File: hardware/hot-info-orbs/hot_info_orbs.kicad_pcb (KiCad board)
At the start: 2 copper layers, 198.8 x 28.5 mm, 11 parts, among them SW1 SW_Push, SW2 SW_Push, SW3 SW_Push, U2 ESP32-S3-SuperMini

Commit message: Board fixes: DS5 DC connected, button off the strapping pin, GND pour added
Three changes to Yang's Rev 1.0, all verified against the file and by re-running
KiCad's own checks -- ERC 0, DRC 0, 0 unconnected pads, 0 schematic parity
issues, and the three silkscreen warnings cleared too.

DS5 pin 5 (DC) now lands on Net-(DS1-DC). The wire had been drawn but stopped
3.81mm short of the pin, so the fifth display had no data/command line. Worth
noting DRC could never have caught it: the board faithfully implemented the
schematic, and the gap was in the schematic. Only ERC sees that class.

SW3 moved from GPIO3 to GPIO10. GPIO3 is an ESP32-S3 strapping pin and the
buttons pull high, so holding that button during a reset drove a strapping pin
at boot -- the shape of an intermittent no-boot nobody traces to a button.
GPIO10 was already broken out and unused.

GND pour on B.Cu, and a SECOND antenna keepout added on B.Cu. The original
keepout was F.Cu only and set to copperpour allowed, so a back-side pour would
have filled straight under the SuperMini's antenna -- the one thing the keepout
exists to prevent. Both layers now exclude copper fill.

Vias went 20 -> 21 rather than down, because the original GND traces remain
alongside the pour. Deliberately not rerouting: via count only mattered while
milling was under consideration, and this board is going to JLCPCB where vias
are free. Wholesale rerouting someone else's board is also far harder to review
than three targeted fixes.
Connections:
- DS5 pad 5: unconnected-(DS5-DC-Pad5) -> Net-(DS1-DC)
- SW3 pad 1: Net-(U2-GPIO_3) -> /SW3
- U2 pad 14: Net-(U2-GPIO_3) -> unconnected-(U2-GPIO_3-Pad14)
- U2 pad 7: unconnected-(U2-GPIO_10-Pad7) -> /SW3
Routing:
- net Net-(DS1-DC): track 129.4 -> 254.5 mm
- net /SW3: track 0.00 -> 111.3 mm, vias 0 -> 2
- net Net-(U2-GPIO_3): track 93.9 -> 0.00 mm, vias 1 -> 0
- added copper zone on B.Cu, net GND

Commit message: Yang's v2: near-complete reroute, DS5 fixed, real logo library, 3D models
Second board from Yang, received while we were fixing the first. He reworked
the routing substantially -- 192 of 211 track segments removed and 197 added,
against 19 segments in common with our version -- and moved signal copper onto
F.Cu, dropping B.Cu from 309mm to 221mm. That leaves the back layer clearer
than v1 did, which suits the ground pour better than his original would have.

He fixed DS5's DC pin independently. He did not move the button off GPIO3 and
did not add a pour, so those two of our three changes still need re-applying
on top of this; that is the next commit rather than this one, so his work and
ours stay separable in the history.

This commit takes his board wholesale rather than merging: KiCad files do not
merge, and reproducing his reroute would cost far more than re-applying two
well-understood edits.

Also brings the Hot_Logo_5x5mm library he had omitted from the first zip --
replacing the copy recovered out of the board cache -- plus STEP models for the
SuperMini and the display.

3D model paths rewritten from ${KICAD_USER_3DMODEL_DIR} to ${KIPRJMOD}/lib/3d.
His pointed at a directory on his own machine, the same portability problem the
symbol and footprint libraries had. Models do not affect fabrication, but a
project that renders for one person and not the other is the thing this layout
was set up to avoid.
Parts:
- C1: value C_Polarized_Small_US -> 100uf
- moved C1 17.8 mm to (116.2, 100.1), turned to 180 degrees
- moved U2 4.72 mm to (131.1, 95.9), turned to 0 degrees
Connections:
- SW3 pad 1: /SW3 -> Net-(U2-GPIO_3)
- U2 pad 14: unconnected-(U2-GPIO_3-Pad14) -> Net-(U2-GPIO_3)
- U2 pad 7: /SW3 -> unconnected-(U2-GPIO_10-Pad7)
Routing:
- net /SW3: track 111.3 -> 0.00 mm, vias 2 -> 0
- net Net-(U2-GPIO_3): track 0.00 -> 102.4 mm
- net Net-(DS1-DC): track 254.5 -> 181.2 mm
- net Net-(U2-3V3): track 117.4 -> 86.9 mm, vias 1 -> 0
- net Net-(DS5-CS): track 109.6 -> 88.3 mm, vias 1 -> 0
- net Net-(DS4-CS): track 53.8 -> 70.0 mm, vias 1 -> 2
- net Net-(DS2-CS): track 33.3 -> 18.1 mm
- net Net-(DS3-CS): track 9.41 -> 24.6 mm
- net GND: track 195.9 -> 181.4 mm, vias 4 -> 2
- net +5V: track 195.0 -> 182.2 mm, vias 0 -> 1
- net Net-(DS1-CS): track 72.8 -> 61.8 mm, vias 0 -> 2
- net Net-(DS1-SCL): track 177.7 -> 170.2 mm, vias 3 -> 2
- net Net-(DS1-RST): track 166.0 -> 171.0 mm, vias 1 -> 3
- net Net-(U2-GPIO_2): track 83.4 -> 87.2 mm, vias 1 -> 0
- net Net-(DS1-SDA): track 172.8 -> 171.3 mm, vias 3 -> 2
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- removed copper zone on B.Cu, net GND
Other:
- board text added: "Based on https://github.com/brettdottech/info-orbs"
- board text added: "HoT Info Orbs Rev 1.1"
- board text removed: "HoT Info Orbs Rev 1.0"
- board text removed: "THIS SIDE UP"

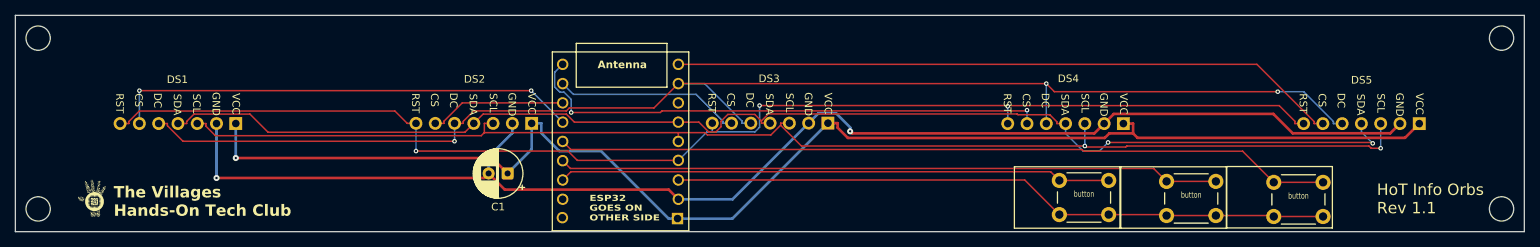
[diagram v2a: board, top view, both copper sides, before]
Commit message: Re-apply our changes onto Yang's v2, and drop the now-stale fab package
Onto his board: GND pour on B.Cu, a B.Cu antenna keepout, both keepouts set to
copperpour not_allowed, and the JLCPCB design rules his .kicad_pro had back at
0.0 clearance and track width.

I got the keepout wrong first and it is worth recording why. I transplanted the
B.Cu keepout from our earlier board, which put it 18mm from the antenna, and
DRC duly reported one of Yang's +5V tracks as forbidden copper. The track was
fine; my keepout was in the wrong place.

The cause is the interesting part: **Yang rotated and moved the module in v2**,
from (131.06, 91.17) at rot=180 to (131.10, 95.89) at rot=0. He moved his F.Cu
keepout to match. Anything positional lifted from the older board is therefore
misplaced by construction. The B.Cu keepout is now derived from HIS current
F.Cu one, so the two are identical outlines on opposite layers and stay correct
if he moves the module again.

Zone fills are stripped rather than transplanted: a fill computed against our
old routing would have looked plausible and been wrong. KiCad recomputes on
open.

Generated gerbers deleted. They describe the pre-v2 board and the board is not
final -- zones are unfilled and the GPIO3 button move still needs doing in the
schematic. fab/README says how to regenerate.

Consequence worth chasing with Yang: he told us the 3D-printed case needs
modifying because he had spun the SuperMini so USB exits the back. He has now
changed that orientation again, so whatever case modification he described may
no longer be the right one.
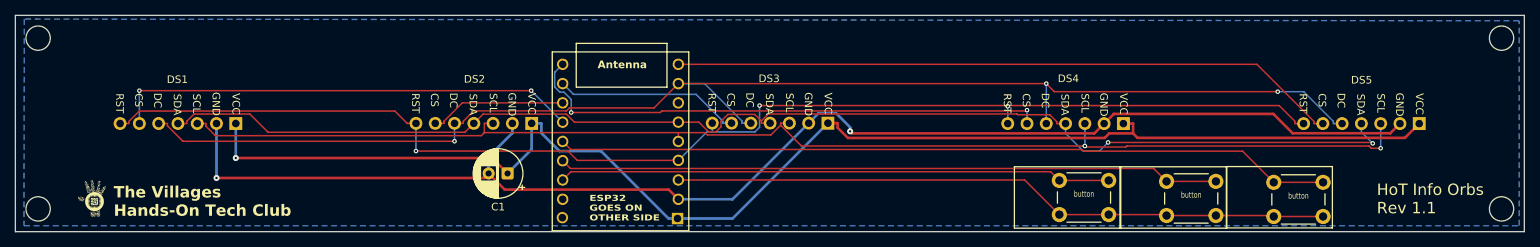
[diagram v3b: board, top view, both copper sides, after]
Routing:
- added copper zone on B.Cu, net GND
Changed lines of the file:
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@@
 			(vias not_allowed)
 			(pads not_allowed)
-			(copperpour allowed)
+			(copperpour not_allowed)
 			(footprints allowed)
 		)
@@
 	)
 	(embedded_fonts no)
+	(zone
+		(net "GND")
+		(layer "B.Cu")
+		(name "GND")
+		(hatch edge 0.5)
+		(connect_pads
+			(clearance 0)
+		)
+		(min_thickness 0.25)
+		(fill yes
+			(thermal_gap 0.5)
+			(thermal_bridge_width 0.5)
+			(island_removal_mode 0)
+		)
+		(polygon
+			(pts
+				(xy 52.532697 79.763543) (xy 52.5 107) (xy 249.5 107) (xy 249.5 80)
+			)
+		)
+	)
+	(zone
+		(layer "B.Cu")
+		(uuid "b0000000-0000-4000-8000-00000000cu2b")
+		(name "Antenna Keep Out")
+		(hatch edge 0.5)
+		(connect_pads
+			(clearance 0)
+		)
+		(min_thickness 0.25)
+		(keepout
+			(tracks not_allowed)
+			(vias not_allowed)
+			(pads not_allowed)
+			(copperpour not_allowed)
+			(footprints allowed)
+		)
+		(placement
+			(enabled no)
+			(sheetname "")
+		)
+		(fill
+			(thermal_gap 0.5)
+			(thermal_bridge_width 0.5)
+			(island_removal_mode 0)
+		)
+		(polygon
+			(pts
+				(xy 125.31 83.04) (xy 137.12232 82.981493) (xy 137.15 88.57) (xy 125.31 88.59) (xy 125.34 83.05)
+			)
+		)
+	)
 )

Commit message: v1.1 first production run: SW3 to GPIO10, pour filled, gerbers generated
Board is Yang's v1.1 with the three changes settled: SW3 moved off GPIO3, which
is an ESP32-S3 strapping pin the buttons would have driven high at reset;
GPIO3 now unconnected and GPIO10 carries the button. GND pour on B.Cu, filled.
Antenna keepout mirrored onto B.Cu and both layers set to block copper fill --
his original was F.Cu only and allowed the pour, which would have flooded copper
under the antenna the keepout exists to protect. Yang's leftover 3.81mm wire
stub from his own DS5 fix is gone.

Verified rather than assumed: ERC 0, DRC 0 unconnected pads, 0 schematic parity
issues. One silkscreen overlap on B.Silkscreen near U2 accepted as cosmetic.

Drill file cross-checks exactly against the footprints -- 18 vias at 0.30, 2 at
0.80 for C1, 53 at 1.00 for the display headers and module pins, 12 at 1.10 for
the buttons, 85 total. The four mounting holes are absent by design; they are
Edge.Cuts circles the fab routes.

The zip is named for the run and is not to be regenerated. If the board changes
the next run gets its own zip and tag, and this one stays byte-identical to what
was ordered -- so that when a board comes back there is no question what was
sent.

Carried knowingly into this run: 0.6/0.3 vias give a 0.150mm annular ring
against JLCPCB's stated 0.18mm. Recorded in fab/README as the first thing to
examine if these boards have via problems.
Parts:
- C1: value 100uf -> C_Polarized_Small_US
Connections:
- SW3 pad 1: Net-(U2-GPIO_3) -> /SW3
- U2 pad 14: Net-(U2-GPIO_3) -> unconnected-(U2-GPIO_3-Pad14)
- U2 pad 7: unconnected-(U2-GPIO_10-Pad7) -> /SW3
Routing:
- net Net-(U2-GPIO_3): track 102.4 -> 0.00 mm
- net /SW3: track 0.00 -> 96.9 mm, vias 0 -> 1
